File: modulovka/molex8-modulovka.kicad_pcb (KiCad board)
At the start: 2 copper layers, 43 x 40 mm, 7 parts, among them J1 Conn_01x04, J2 Conn_02x04_Counter_Clockwise, J3 Conn_01x04

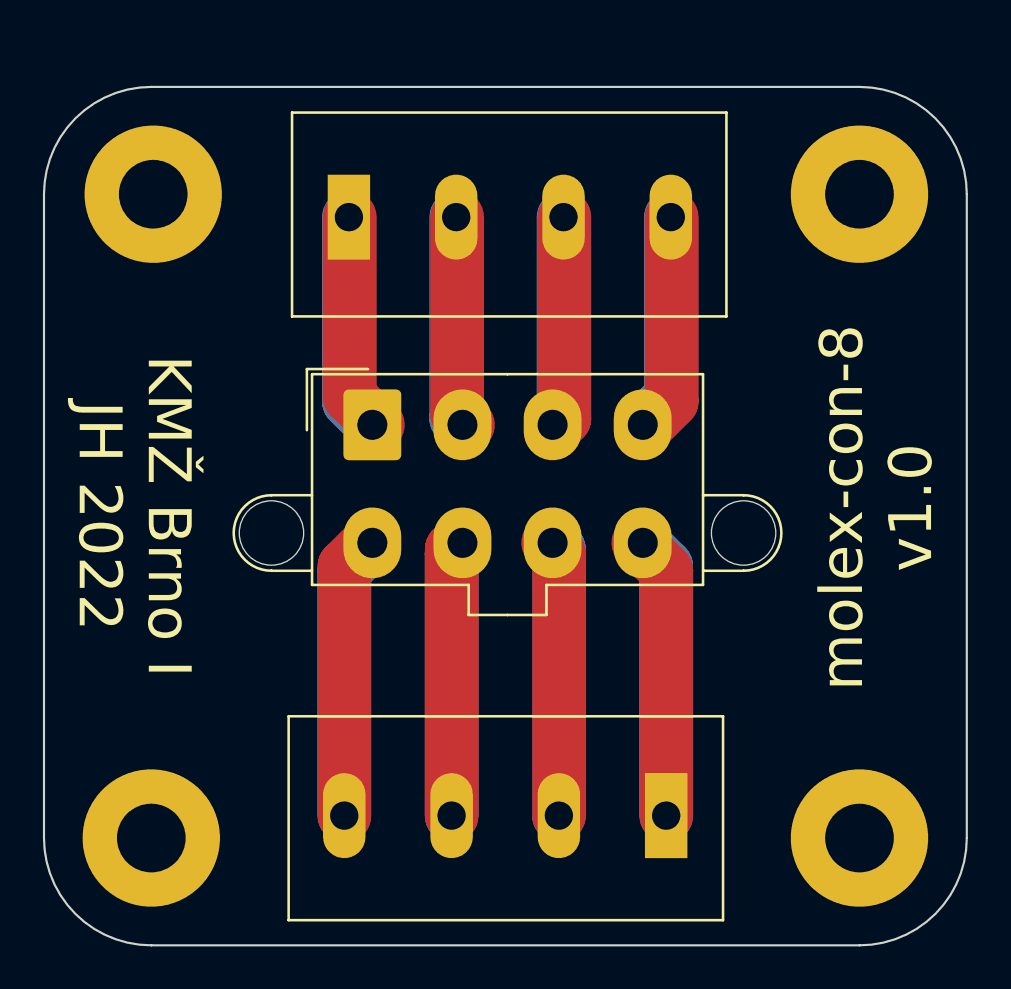
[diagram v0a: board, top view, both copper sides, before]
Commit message: Customize modulovka pcb.
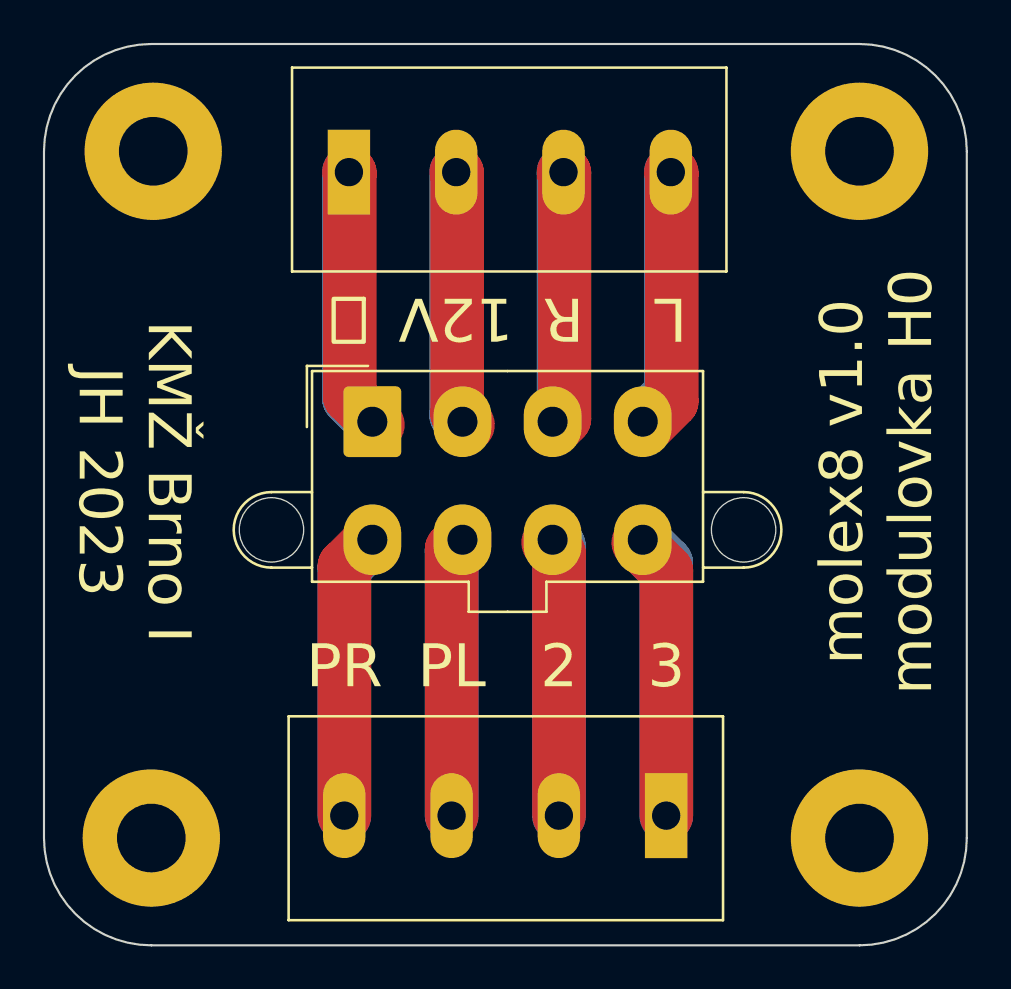
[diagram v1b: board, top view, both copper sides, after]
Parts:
- moved J1 2.10 mm to (101.6, 80.2)
- moved H1 2.00 mm to (85.1, 79.0)
- moved H4 2.00 mm to (118.0, 79.0)
- moved J2 0.15 mm to (95.3, 91.6)
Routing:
- net Net-(J1-Pad4): track 20.4 -> 24.4 mm
- net Net-(J1-Pad2): track 19.7 -> 23.7 mm
- net Net-(J1-Pad3): track 19.7 -> 23.7 mm
- net Net-(J1-Pad1): track 20.4 -> 24.4 mm
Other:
- board size 43 x 40 mm -> 43 x 42 mm
- board text added: "12V"
- board text added: "2"
- board text added: "3"
- board text added: "KMŽ Brno I JH 2023"
- board text added: "L"
- board text added: "PL"
- board text added: "PR"
- board text added: "R"
- board text added: "molex8 v1.0 modulovka H0"
- board text added: "⏚"
- board text removed: "KMŽ Brno I JH 2022"
- board text removed: "molex-con-8 v1.0"

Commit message: Standardize dimensions to 42x42 mm.
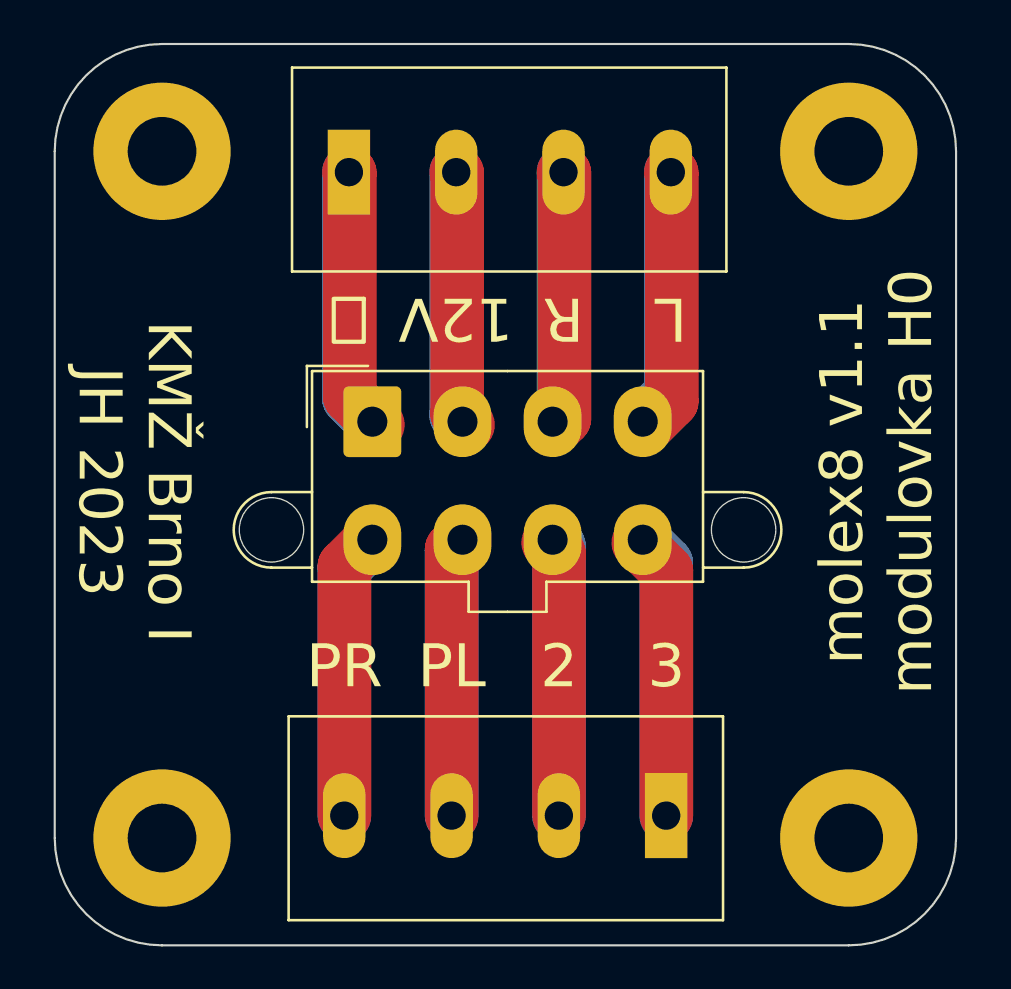
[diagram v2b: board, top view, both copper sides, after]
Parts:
- moved H2 0.50 mm to (117.5, 111.0)
- moved H3 0.50 mm to (85.5, 111.0)
- moved H4 0.50 mm to (117.5, 79.0)
- moved H1 0.41 mm to (85.5, 79.0)
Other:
- board size 43 x 42 mm -> 42 x 42 mm
- board text added: "molex8 v1.1 modulovka H0"
- board text removed: "molex8 v1.0 modulovka H0"
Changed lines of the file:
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@@
   )
   (footprint "MountingHole:MountingHole_3.2mm_M3_Pad" (layer "F.Cu")
-    (at 85.09 79)
+    (at 85.5 79)
     (descr "Mounting Hole 3.2mm, M3")
     (tags "mounting hole 3.2mm m3")
@@
   )
   (footprint "MountingHole:MountingHole_3.2mm_M3_Pad" (layer "F.Cu")
-    (at 118 79)
+    (at 117.5 79)
     (descr "Mounting Hole 3.2mm, M3")
     (tags "mounting hole 3.2mm m3")
@@
   )
   (footprint "MountingHole:MountingHole_3.2mm_M3_Pad" (layer "F.Cu")
-    (at 118 111)
+    (at 117.5 111)
     (descr "Mounting Hole 3.2mm, M3")
     (tags "mounting hole 3.2mm m3")
@@
   )
   (footprint "MountingHole:MountingHole_3.2mm_M3_Pad" (layer "F.Cu")
-    (at 85 111)
+    (at 85.5 111)
     (descr "Mounting Hole 3.2mm, M3")
     (tags "mounting hole 3.2mm m3")
@@
   (gr_line (start 109 110) (end 109 98.25) (layer "B.Mask") (width 2.5))
   (gr_line (start 94 98.75) (end 95.25 97.25) (layer "B.Mask") (width 2.5))
-  (gr_arc (start 118 74) (mid 121.535534 75.464466) (end 123 79) (layer "Edge.Cuts") (width 0.1))
-  (gr_arc (start 80 79) (mid 81.464466 75.464466) (end 85 74) (layer "Edge.Cuts") (width 0.1))
-  (gr_line (start 118 116) (end 85 116) (layer "Edge.Cuts") (width 0.1))
-  (gr_line (start 80 111) (end 80 79) (layer "Edge.Cuts") (width 0.1))
-  (gr_line (start 85 74) (end 118 74) (layer "Edge.Cuts") (width 0.1))
-  (gr_line (start 123 79) (end 123 111) (layer "Edge.Cuts") (width 0.1))
-  (gr_arc (start 85 116) (mid 81.464466 114.535534) (end 80 111) (layer "Edge.Cuts") (width 0.1))
-  (gr_arc (start 123 111) (mid 121.535534 114.535534) (end 118 116) (layer "Edge.Cuts") (width 0.1))
+  (gr_arc (start 117.5 74) (mid 121.035534 75.464466) (end 122.5 79) (layer "Edge.Cuts") (width 0.1))
+  (gr_arc (start 80.5 79) (mid 81.964466 75.464466) (end 85.5 74) (layer "Edge.Cuts") (width 0.1))
+  (gr_line (start 117.5 116) (end 85.5 116) (layer "Edge.Cuts") (width 0.1))
+  (gr_line (start 80.5 111) (end 80.5 79) (layer "Edge.Cuts") (width 0.1))
+  (gr_line (start 85.5 74) (end 117.5 74) (layer "Edge.Cuts") (width 0.1))
+  (gr_line (start 122.5 79) (end 122.5 111) (layer "Edge.Cuts") (width 0.1))
+  (gr_arc (start 85.5 116) (mid 81.964466 114.535534) (end 80.5 111) (layer "Edge.Cuts") (width 0.1))
+  (gr_arc (start 122.5 111) (mid 121.035534 114.535534) (end 117.5 116) (layer "Edge.Cuts") (width 0.1))
   (gr_text "R" (at 104.2 86.8 180) (layer "F.SilkS")
     (effects (font (size 2 2) (thickness 0.2)))
@@
     (effects (font (size 2 2) (thickness 0.2)))
   )
-  (gr_text "molex8 v1.0\nmodulovka H0" (at 118.8 94.4 90) (layer "F.SilkS")
-    (effects (font (size 2 2) (thickness 0.2)))
-  )
+  (gr_text "molex8 v1.1\nmodulovka H0" (at 118.8 94.4 90) (layer "F.SilkS")
+    (effects (font (size 2 2) (thickness 0.2)))
+  )

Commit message: Use screw terminal symbols, use MVE25-5-V as values.
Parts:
- H1, H2, H3, H4: value MountingHole -> MountingHole-3.2mm
- J1, J3: value Conn_01x04 -> 2xMVE252-5-V
- J2: value Conn_02x04_Counter_Clockwise -> TME 39281083 MOLEX
